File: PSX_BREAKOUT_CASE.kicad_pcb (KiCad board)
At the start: 2 copper layers, 100 x 71.1 mm, 11 parts

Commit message: Fixing Merging Error
Updated Case, moved connector, generated gerbers
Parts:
- removed the REF** at (118.4, 44.6)
- removed the REF** at (161.5, 44.8)
- removed the REF** at (178.0, 51.9)
- removed the REF** at (98.5, 62.7)
- added REF**: MountingHole_3.2mm_M3, MountingHole:MountingHole_3.2mm_M3, F.Cu at (162.2, 56.8)
- added REF**: MountingHole_3.2mm_M3, MountingHole:MountingHole_3.2mm_M3, F.Cu at (146.3, 45.6)
- added REF**: MountingHole_3.2mm_M3, MountingHole:MountingHole_3.2mm_M3, F.Cu at (109.7, 61.1)
- added REF**: MountingHole_3.2mm_M3, MountingHole:MountingHole_3.2mm_M3, F.Cu at (107.4, 45.8)
- moved REF** 16.6 mm to (162.2, 92.3)
- moved REF** 15.3 mm to (146.3, 81.2)
- moved REF** 11.4 mm to (109.7, 96.6)
- moved REF** 11.0 mm to (107.4, 81.4)
- moved G*** 10.7 mm to (129.3, 88.4)
- moved REF** 0.76 mm to (140.0, 59.4)
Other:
- outline, holes or cut-outs redrawn
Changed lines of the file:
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@@
-(kicad_pcb (version 20171130) (host pcbnew "(5.1.2)-1")
+(kicad_pcb (version 20171130) (host pcbnew "(5.1.0)-1")
   (general
     (thickness 1.6)
@@
       (drillshape 0)
       (scaleselection 1)
-      (outputdirectory "Gerbers/Case/"))
+      (outputdirectory "Gerbers/"))
   )
   (net 0 "")
@@
     (uvia_drill 0.1)
   )
+  (module MountingHole:MountingHole_3.2mm_M3 (layer F.Cu)
+    (at 162.179 56.769)
+    (descr "Mounting Hole 3.2mm, no annular, M3")
+    (tags "mounting hole 3.2mm no annular m3")
+    (attr virtual)
+    (fp_text reference REF** (at 0 -4.2) (layer F.SilkS) hide
+      (effects (font (size 1 1) (thickness 0.15)))
+    )
+    (fp_text value MountingHole_3.2mm_M3 (at 0 4.2) (layer F.Fab)
+      (effects (font (size 1 1) (thickness 0.15)))
+    )
+    (fp_text user %R (at 0.3 0) (layer F.Fab)
+      (effects (font (size 1 1) (thickness 0.15)))
+    )
+    (fp_circle (center 0 0) (end 3.2 0) (layer Cmts.User) (width 0.15))
+    (fp_circle (center 0 0) (end 3.45 0) (layer F.CrtYd) (width 0.05))
+    (pad 1 np_thru_hole circle (at 0 0) (size 3.2 3.2) (drill 3.2) (layers *.Cu *.Mask))
+  )
+  (module MountingHole:MountingHole_3.2mm_M3 (layer F.Cu)
+    (at 146.304 45.593)
+    (descr "Mounting Hole 3.2mm, no annular, M3")
+    (tags "mounting hole 3.2mm no annular m3")
+    (attr virtual)
+    (fp_text reference REF** (at 0 -4.2) (layer F.SilkS) hide
+      (effects (font (size 1 1) (thickness 0.15)))
+    )
+    (fp_text value MountingHole_3.2mm_M3 (at 0 4.2) (layer F.Fab)
+      (effects (font (size 1 1) (thickness 0.15)))
+    )
+    (fp_circle (center 0 0) (end 3.45 0) (layer F.CrtYd) (width 0.05))
+    (fp_circle (center 0 0) (end 3.2 0) (layer Cmts.User) (width 0.15))
+    (fp_text user %R (at 0.3 0) (layer F.Fab)
+      (effects (font (size 1 1) (thickness 0.15)))
+    )
+    (pad 1 np_thru_hole circle (at 0 0) (size 3.2 3.2) (drill 3.2) (layers *.Cu *.Mask))
+  )
+  (module MountingHole:MountingHole_3.2mm_M3 (layer F.Cu)
+    (at 109.728 61.087)
+    (descr "Mounting Hole 3.2mm, no annular, M3")
+    (tags "mounting hole 3.2mm no annular m3")
+    (attr virtual)
+    (fp_text reference REF** (at 0 -4.2) (layer F.SilkS) hide
+      (effects (font (size 1 1) (thickness 0.15)))
+    )
+    (fp_text value MountingHole_3.2mm_M3 (at 0 4.2) (layer F.Fab)
+      (effects (font (size 1 1) (thickness 0.15)))
+    )
+    (fp_circle (center 0 0) (end 3.45 0) (layer F.CrtYd) (width 0.05))
+    (fp_circle (center 0 0) (end 3.2 0) (layer Cmts.User) (width 0.15))
+    (fp_text user %R (at 0.3 0) (layer F.Fab)
+      (effects (font (size 1 1) (thickness 0.15)))
+    )
+    (pad 1 np_thru_hole circle (at 0 0) (size 3.2 3.2) (drill 3.2) (layers *.Cu *.Mask))
+  )
+  (module MountingHole:MountingHole_3.2mm_M3 (layer F.Cu)
+    (at 107.442 45.847)
+    (descr "Mounting Hole 3.2mm, no annular, M3")
+    (tags "mounting hole 3.2mm no annular m3")
+    (attr virtual)
+    (fp_text reference REF** (at 0 -4.2) (layer F.SilkS) hide
+      (effects (font (size 1 1) (thickness 0.15)))
+    )
+    (fp_text value MountingHole_3.2mm_M3 (at 0 4.2) (layer F.Fab)
+      (effects (font (size 1 1) (thickness 0.15)))
+    )
+    (fp_text user %R (at 0.3 0) (layer F.Fab)
+      (effects (font (size 1 1) (thickness 0.15)))
+    )
+    (fp_circle (center 0 0) (end 3.2 0) (layer Cmts.User) (width 0.15))
+    (fp_circle (center 0 0) (end 3.45 0) (layer F.CrtYd) (width 0.05))
+    (pad 1 np_thru_hole circle (at 0 0) (size 3.2 3.2) (drill 3.2) (layers *.Cu *.Mask))
+  )
   (module PSX_BREAKOUT:PSX_LOGO (layer F.Cu)
-    (at 139.954 88.44)
+    (at 129.286 88.44)
     (fp_text reference G*** (at 0 0) (layer F.SilkS) hide
       (effects (font (size 1.524 1.524) (thickness 0.3)))
@@
   )
   (module Symbol:OSHW-Symbol_33.5x30mm_Copper (layer B.Cu)
-    (at 139.954 58.674 180)
+    (at 139.954 59.436 180)
     (descr "Open Source Hardware Symbol")
     (tags "Logo Symbol OSHW")
@@
   )
   (module MountingHole:MountingHole_3.2mm_M3 (layer F.Cu)
-    (at 118.364 44.577)
+    (at 109.728 96.647)
     (descr "Mounting Hole 3.2mm, no annular, M3")
     (tags "mounting hole 3.2mm no annular m3")
@@
   )
   (module MountingHole:MountingHole_3.2mm_M3 (layer F.Cu)
-    (at 161.544 44.831)
+    (at 107.442 81.407)
     (descr "Mounting Hole 3.2mm, no annular, M3")
     (tags "mounting hole 3.2mm no annular m3")
@@
   )
   (module MountingHole:MountingHole_3.2mm_M3 (layer F.Cu)
-    (at 178.016 51.943)
+    (at 146.304 81.153)
     (descr "Mounting Hole 3.2mm, no annular, M3")
     (tags "mounting hole 3.2mm no annular m3")
@@
   )
   (module MountingHole:MountingHole_3.2mm_M3 (layer F.Cu)
-    (at 98.463 62.738)
+    (at 162.179 92.329)
     (descr "Mounting Hole 3.2mm, no annular, M3")
     (tags "mounting hole 3.2mm no annular m3")
@@
     (pad 1 np_thru_hole circle (at 0 0) (size 3.2 3.2) (drill 3.2) (layers *.Cu *.Mask))
   )
-  (module MountingHole:MountingHole_3.2mm_M3 (layer F.Cu)
-    (at 98.463 98.298)
-    (descr "Mounting Hole 3.2mm, no annular, M3")
-    (tags "mounting hole 3.2mm no annular m3")
-    (attr virtual)
-    (fp_text reference REF** (at 0 -4.2) (layer F.SilkS) hide
-      (effects (font (size 1 1) (thickness 0.15)))
-    )
-    (fp_text value MountingHole_3.2mm_M3 (at 0 4.2) (layer F.Fab)
-      (effects (font (size 1 1) (thickness 0.15)))
-    )
-    (fp_text user %R (at 0.3 0) (layer F.Fab)
-      (effects (font (size 1 1) (thickness 0.15)))
-    )
-    (fp_circle (center 0 0) (end 3.2 0) (layer Cmts.User) (width 0.15))
-    (fp_circle (center 0 0) (end 3.45 0) (layer F.CrtYd) (width 0.05))
-    (pad 1 np_thru_hole circle (at 0 0) (size 3.2 3.2) (drill 3.2) (layers *.Cu *.Mask))
-  )
-  (module MountingHole:MountingHole_3.2mm_M3 (layer F.Cu)
-    (at 118.364 80.137)
-    (descr "Mounting Hole 3.2mm, no annular, M3")
-    (tags "mounting hole 3.2mm no annular m3")
-    (attr virtual)
-    (fp_text reference REF** (at 0 -4.2) (layer F.SilkS) hide
-      (effects (font (size 1 1) (thickness 0.15)))
-    )
-    (fp_text value MountingHole_3.2mm_M3 (at 0 4.2) (layer F.Fab)
-      (effects (font (size 1 1) (thickness 0.15)))
-    )
-    (fp_circle (center 0 0) (end 3.45 0) (layer F.CrtYd) (width 0.05))
-    (fp_circle (center 0 0) (end 3.2 0) (layer Cmts.User) (width 0.15))
-    (fp_text user %R (at 0.3 0) (layer F.Fab)
-      (effects (font (size 1 1) (thickness 0.15)))
-    )
-    (pad 1 np_thru_hole circle (at 0 0) (size 3.2 3.2) (drill 3.2) (layers *.Cu *.Mask))
-  )
-  (module MountingHole:MountingHole_3.2mm_M3 (layer F.Cu)
-    (at 161.544 80.391)
-    (descr "Mounting Hole 3.2mm, no annular, M3")
-    (tags "mounting hole 3.2mm no annular m3")
-    (attr virtual)
-    (fp_text reference REF** (at 0 -4.2) (layer F.SilkS) hide
-      (effects (font (size 1 1) (thickness 0.15)))
-    )
-    (fp_text value MountingHole_3.2mm_M3 (at 0 4.2) (layer F.Fab)
-      (effects (font (size 1 1) (thickness 0.15)))
-    )
-    (fp_text user %R (at 0.3 0) (layer F.Fab)
-      (effects (font (size 1 1) (thickness 0.15)))
-    )
-    (fp_circle (center 0 0) (end 3.2 0) (layer Cmts.User) (width 0.15))
-    (fp_circle (center 0 0) (end 3.45 0) (layer F.CrtYd) (width 0.05))
-    (pad 1 np_thru_hole circle (at 0 0) (size 3.2 3.2) (drill 3.2) (layers *.Cu *.Mask))
-  )
-  (module MountingHole:MountingHole_3.2mm_M3 (layer F.Cu)
-    (at 178.016 87.503)
-    (descr "Mounting Hole 3.2mm, no annular, M3")
-    (tags "mounting hole 3.2mm no annular m3")
-    (attr virtual)
-    (fp_text reference REF** (at 0 -4.2) (layer F.SilkS) hide
-      (effects (font (size 1 1) (thickness 0.15)))
-    )
-    (fp_text value MountingHole_3.2mm_M3 (at 0 4.2) (layer F.Fab)
-      (effects (font (size 1 1) (thickness 0.15)))
-    )
-    (fp_circle (center 0 0) (end 3.45 0) (layer F.CrtYd) (width 0.05))
-    (fp_circle (center 0 0) (end 3.2 0) (layer Cmts.User) (width 0.15))
-    (fp_text user %R (at 0.3 0) (layer F.Fab)
-      (effects (font (size 1 1) (thickness 0.15)))
-    )
-    (pad 1 np_thru_hole circle (at 0 0) (size 3.2 3.2) (drill 3.2) (layers *.Cu *.Mask))
-  )
-  (gr_line (start 147.9735 97.26) (end 147.9735 111.76) (layer Edge.Cuts) (width 0.05))
-  (gr_line (start 189.954 97.26) (end 147.9735 97.26) (layer Edge.Cuts) (width 0.05))
+  (gr_line (start 147.9735 99.26) (end 147.9735 111.76) (layer Edge.Cuts) (width 0.05))
+  (gr_line (start 189.954 99.26) (end 147.9735 99.26) (layer Edge.Cuts) (width 0.05))
   (gr_line (start 132.461 40.64) (end 107.95 40.64) (layer Edge.Cuts) (width 0.05))
   (gr_line (start 132.461 40.64) (end 165.735 40.64) (layer Edge.Cuts) (width 0.05))
@@
     (effects (font (size 3 3) (thickness 0.15)))
   )
-  (gr_text 75Ω (at 110.236 77.724) (layer F.SilkS)
+  (gr_text 75Ω (at 125.476 77.724) (layer F.SilkS)
     (effects (font (size 1 1) (thickness 0.15)))
   )
-  (gr_text TTL (at 105.283 77.724) (layer F.SilkS)
+  (gr_text TTL (at 120.523 77.724) (layer F.SilkS)
     (effects (font (size 1 1) (thickness 0.15)))
   )
-  (gr_text "Sync Select\n↑CVBS\n●CSYNC\n↓LUMA" (at 156.591 90.17) (layer F.SilkS)
+  (gr_text "Sync Select\n↑CVBS\n●CSYNC\n↓LUMA" (at 166.878 87.122) (layer F.SilkS)
     (effects (font (size 2 2) (thickness 0.15)) (justify left))
   )
@@
   (gr_line (start 89.954 76.2) (end 89.954 111.76) (layer Edge.Cuts) (width 0.05))
   (gr_line (start 107.95 76.2) (end 89.954 76.2) (layer Edge.Cuts) (width 0.05))
-  (gr_line (start 189.954 76.2) (end 189.954 97.26) (layer Edge.Cuts) (width 0.05))
+  (gr_line (start 189.954 76.2) (end 189.954 99.26) (layer Edge.Cuts) (width 0.05))
   (gr_line (start 165.735 76.2) (end 189.954 76.2) (layer Edge.Cuts) (width 0.05))
   (gr_line (start 147.9735 111.76) (end 89.954 111.76) (layer Edge.Cuts) (width 0.05))

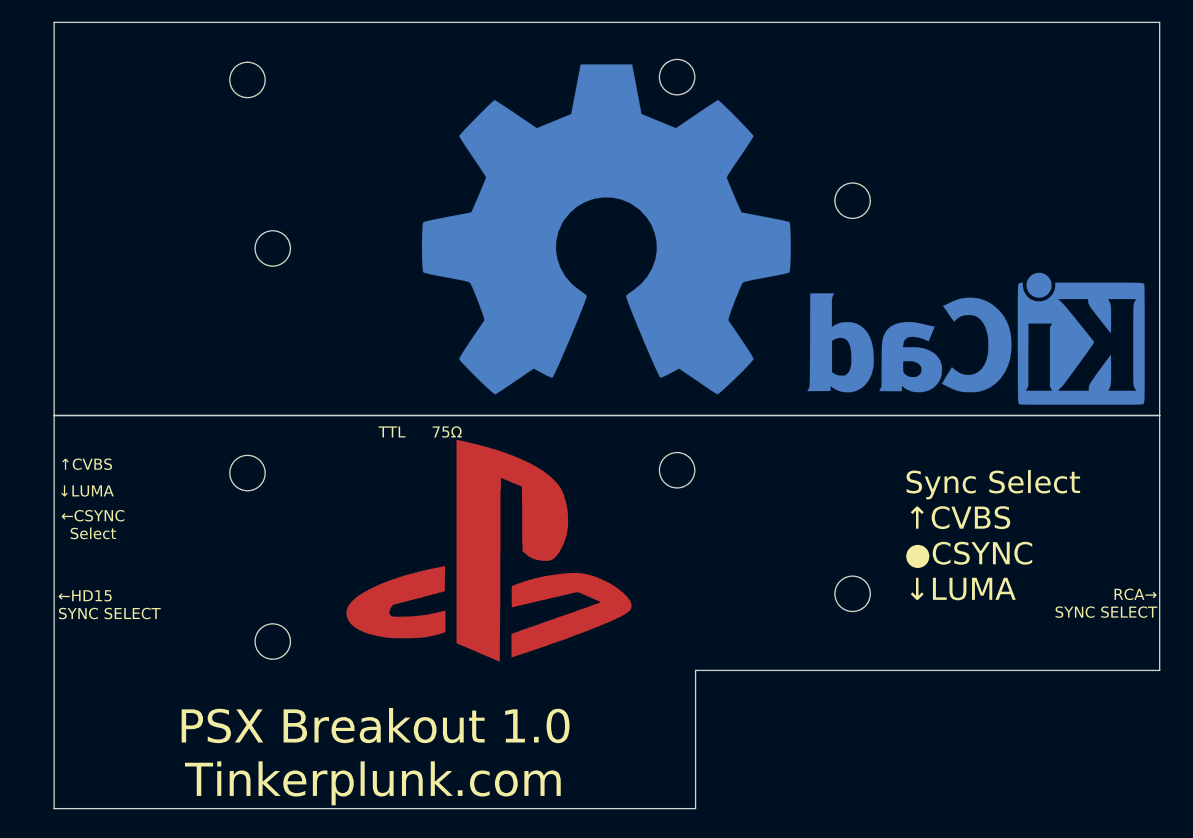
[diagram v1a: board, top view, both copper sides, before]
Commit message: Big Changes
Moved the csync selector switch to the right in order to move the hd15 connector back to the right position. Fixed hd15 footprint, moved screw holes and updated case with new screw holes and input labels. Updated 3d model for HD15 connector.
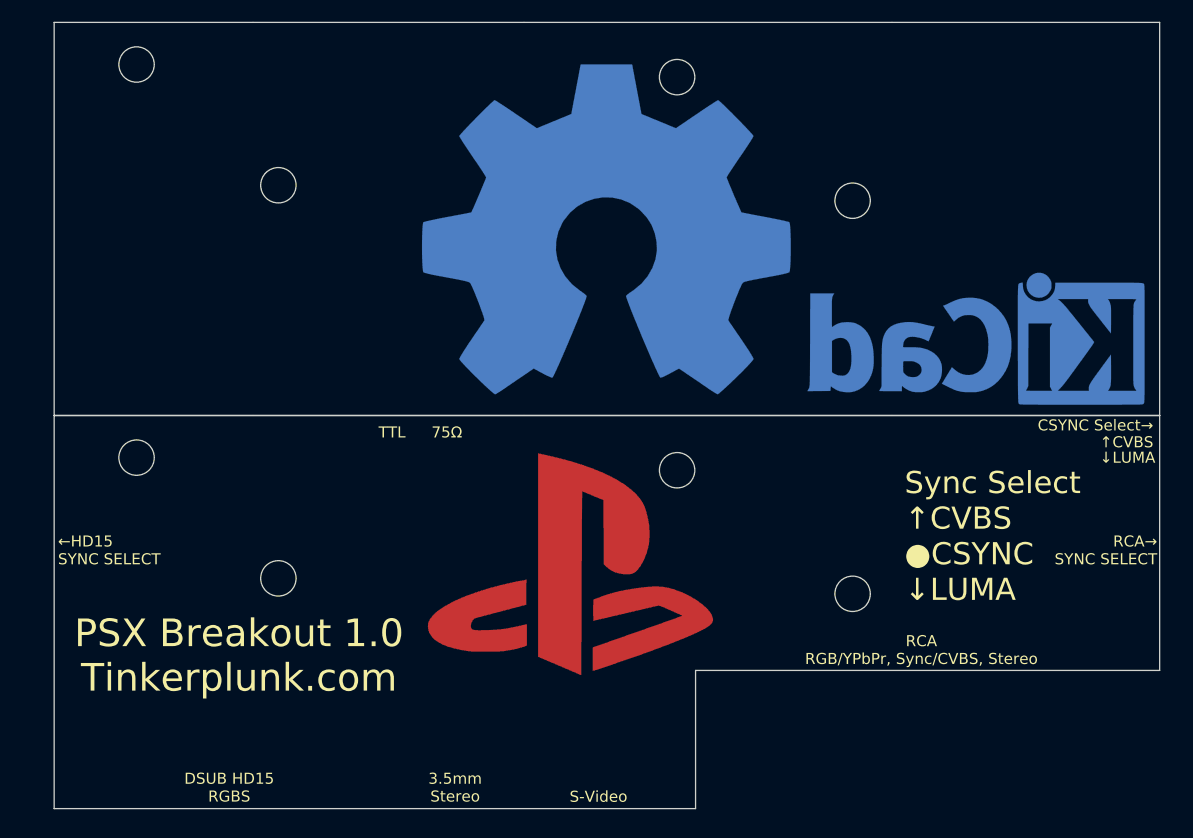
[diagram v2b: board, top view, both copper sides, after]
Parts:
- removed the REF** at (109.7, 61.1)
- removed the REF** at (107.4, 45.8)
- added REF**: MountingHole_3.2mm_M3, MountingHole:MountingHole_3.2mm_M3, F.Cu at (97.4, 44.5)
- added REF**: MountingHole_3.2mm_M3, MountingHole:MountingHole_3.2mm_M3, F.Cu at (110.2, 55.4)
- moved REF** 10.1 mm to (97.4, 80.0)
- moved G*** 7.47 mm to (136.7, 89.7)
- moved REF** 5.74 mm to (110.2, 90.9)
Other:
- board text added: "3.5mm Stereo"
- board text added: "CSYNC Select→"
- board text added: "DSUB HD15 RGBS"
- board text added: "RCA RGB/YPbPr, Sync/CVBS, Stereo"
- board text added: "S-Video"
- board text added: "←V-Score"
- board text removed: "←CSYNC Select"
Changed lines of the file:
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@@
   (general
     (thickness 1.6)
-    (drawings 26)
+    (drawings 31)
     (tracks 0)
     (zones 0)
@@
     (visible_elements 7FFFFFFF)
     (pcbplotparams
-      (layerselection 0x010f0_ffffffff)
+      (layerselection 0x012f0_ffffffff)
       (usegerberextensions true)
       (usegerberattributes false)
@@
   )
   (module MountingHole:MountingHole_3.2mm_M3 (layer F.Cu)
+    (at 97.409 44.45)
+    (descr "Mounting Hole 3.2mm, no annular, M3")
+    (tags "mounting hole 3.2mm no annular m3")
+    (attr virtual)
+    (fp_text reference REF** (at 0 -4.2) (layer F.SilkS) hide
+      (effects (font (size 1 1) (thickness 0.15)))
+    )
+    (fp_text value MountingHole_3.2mm_M3 (at 0 4.2) (layer F.Fab)
+      (effects (font (size 1 1) (thickness 0.15)))
+    )
+    (fp_text user %R (at 0.3 0) (layer F.Fab)
+      (effects (font (size 1 1) (thickness 0.15)))
+    )
+    (fp_circle (center 0 0) (end 3.2 0) (layer Cmts.User) (width 0.15))
+    (fp_circle (center 0 0) (end 3.45 0) (layer F.CrtYd) (width 0.05))
+    (pad 1 np_thru_hole circle (at 0 0) (size 3.2 3.2) (drill 3.2) (layers *.Cu *.Mask))
+  )
+  (module MountingHole:MountingHole_3.2mm_M3 (layer F.Cu)
+    (at 110.236 55.372)
+    (descr "Mounting Hole 3.2mm, no annular, M3")
+    (tags "mounting hole 3.2mm no annular m3")
+    (attr virtual)
+    (fp_text reference REF** (at 0 -4.2) (layer F.SilkS) hide
+      (effects (font (size 1 1) (thickness 0.15)))
+    )
+    (fp_text value MountingHole_3.2mm_M3 (at 0 4.2) (layer F.Fab)
+      (effects (font (size 1 1) (thickness 0.15)))
+    )
+    (fp_circle (center 0 0) (end 3.45 0) (layer F.CrtYd) (width 0.05))
+    (fp_circle (center 0 0) (end 3.2 0) (layer Cmts.User) (width 0.15))
+    (fp_text user %R (at 0.3 0) (layer F.Fab)
+      (effects (font (size 1 1) (thickness 0.15)))
+    )
+    (pad 1 np_thru_hole circle (at 0 0) (size 3.2 3.2) (drill 3.2) (layers *.Cu *.Mask))
+  )
+  (module MountingHole:MountingHole_3.2mm_M3 (layer F.Cu)
     (at 162.179 56.769)
     (descr "Mounting Hole 3.2mm, no annular, M3")
@@
     (pad 1 np_thru_hole circle (at 0 0) (size 3.2 3.2) (drill 3.2) (layers *.Cu *.Mask))
   )
-  (module MountingHole:MountingHole_3.2mm_M3 (layer F.Cu)
-    (at 109.728 61.087)
-    (descr "Mounting Hole 3.2mm, no annular, M3")
-    (tags "mounting hole 3.2mm no annular m3")
-    (attr virtual)
-    (fp_text reference REF** (at 0 -4.2) (layer F.SilkS) hide
-      (effects (font (size 1 1) (thickness 0.15)))
-    )
-    (fp_text value MountingHole_3.2mm_M3 (at 0 4.2) (layer F.Fab)
-      (effects (font (size 1 1) (thickness 0.15)))
-    )
-    (fp_circle (center 0 0) (end 3.45 0) (layer F.CrtYd) (width 0.05))
-    (fp_circle (center 0 0) (end 3.2 0) (layer Cmts.User) (width 0.15))
-    (fp_text user %R (at 0.3 0) (layer F.Fab)
-      (effects (font (size 1 1) (thickness 0.15)))
-    )
-    (pad 1 np_thru_hole circle (at 0 0) (size 3.2 3.2) (drill 3.2) (layers *.Cu *.Mask))
-  )
-  (module MountingHole:MountingHole_3.2mm_M3 (layer F.Cu)
-    (at 107.442 45.847)
-    (descr "Mounting Hole 3.2mm, no annular, M3")
-    (tags "mounting hole 3.2mm no annular m3")
-    (attr virtual)
-    (fp_text reference REF** (at 0 -4.2) (layer F.SilkS) hide
-      (effects (font (size 1 1) (thickness 0.15)))
-    )
-    (fp_text value MountingHole_3.2mm_M3 (at 0 4.2) (layer F.Fab)
-      (effects (font (size 1 1) (thickness 0.15)))
-    )
-    (fp_text user %R (at 0.3 0) (layer F.Fab)
-      (effects (font (size 1 1) (thickness 0.15)))
-    )
-    (fp_circle (center 0 0) (end 3.2 0) (layer Cmts.User) (width 0.15))
-    (fp_circle (center 0 0) (end 3.45 0) (layer F.CrtYd) (width 0.05))
-    (pad 1 np_thru_hole circle (at 0 0) (size 3.2 3.2) (drill 3.2) (layers *.Cu *.Mask))
-  )
   (module PSX_BREAKOUT:PSX_LOGO (layer F.Cu)
-    (at 129.286 88.44)
+    (at 136.652 89.662)
     (fp_text reference G*** (at 0 0) (layer F.SilkS) hide
       (effects (font (size 1.524 1.524) (thickness 0.3)))
@@
   )
   (module MountingHole:MountingHole_3.2mm_M3 (layer F.Cu)
-    (at 109.728 96.647)
+    (at 110.236 90.932)
     (descr "Mounting Hole 3.2mm, no annular, M3")
     (tags "mounting hole 3.2mm no annular m3")
@@
   )
   (module MountingHole:MountingHole_3.2mm_M3 (layer F.Cu)
-    (at 107.442 81.407)
+    (at 97.409 80.01)
     (descr "Mounting Hole 3.2mm, no annular, M3")
     (tags "mounting hole 3.2mm no annular m3")
@@
     )
     (pad 1 np_thru_hole circle (at 0 0) (size 3.2 3.2) (drill 3.2) (layers *.Cu *.Mask))
+  )
+  (gr_text ←V-Score (at 194.183 76.073) (layer Cmts.User)
+    (effects (font (size 1 1) (thickness 0.15)))
+  )
+  (gr_text "RCA\nRGB/YPbPr, Sync/CVBS, Stereo" (at 168.402 97.409) (layer F.SilkS)
+    (effects (font (size 1 1) (thickness 0.15)))
+  )
+  (gr_text S-Video (at 139.192 110.6805) (layer F.SilkS)
+    (effects (font (size 1 1) (thickness 0.15)))
+  )
+  (gr_text "3.5mm\nStereo" (at 126.227 109.855) (layer F.SilkS)
+    (effects (font (size 1 1) (thickness 0.15)))
+  )
+  (gr_text "DSUB HD15\nRGBS" (at 105.791 109.855) (layer F.SilkS)
+    (effects (font (size 1 1) (thickness 0.15)))
   )
   (gr_line (start 147.9735 99.26) (end 147.9735 111.76) (layer Edge.Cuts) (width 0.05))
@@
   (gr_line (start 189.954 76.2) (end 89.954 76.2) (layer Edge.Cuts) (width 0.05))
   (gr_line (start 107.95 40.64) (end 89.954 40.64) (layer Edge.Cuts) (width 0.05))
-  (gr_text "Licensed under CERN OHL 1.2\nhttps://github.com/arithmaldor" (at 138.684 53.213) (layer B.SilkS)
+  (gr_text "Licensed under CERN OHL 1.2\nhttps://github.com/arithmaldor" (at 116.078 70.358) (layer B.SilkS)
     (effects (font (size 2 2) (thickness 0.15)) (justify mirror))
   )
-  (gr_text "PSX Breakout 1.0\nTinkerplunk.com" (at 118.96375 106.807) (layer F.SilkS)
-    (effects (font (size 3 3) (thickness 0.15)))
+  (gr_text "PSX Breakout 1.0\nTinkerplunk.com" (at 106.68 97.917) (layer F.SilkS)
+    (effects (font (size 2.5 2.5) (thickness 0.15)))
   )
   (gr_text 75Ω (at 125.476 77.724) (layer F.SilkS)
@@
     (effects (font (size 2 2) (thickness 0.15)) (justify left))
   )
-  (gr_text "RCA→\nSYNC SELECT" (at 189.738 93.218) (layer F.SilkS)
+  (gr_text "RCA→\nSYNC SELECT" (at 189.738 88.392) (layer F.SilkS)
     (effects (font (size 1 1) (thickness 0.15)) (justify right))
   )
-  (gr_text "←HD15\nSYNC SELECT" (at 90.297 93.345) (layer F.SilkS)
+  (gr_text "←HD15\nSYNC SELECT" (at 90.297 88.392) (layer F.SilkS)
     (effects (font (size 1 1) (thickness 0.15)) (justify left))
   )
-  (gr_text ↓LUMA (at 92.837 83.058) (layer F.SilkS)
+  (gr_text ↓LUMA (at 184.531 80.01) (layer F.SilkS)
+    (effects (font (size 1 1) (thickness 0.15)) (justify left))
+  )
+  (gr_text "CSYNC Select→" (at 184.15 77.089) (layer F.SilkS)
     (effects (font (size 1 1) (thickness 0.15)))
   )
-  (gr_text "←CSYNC\nSelect" (at 93.472 86.106) (layer F.SilkS)
-    (effects (font (size 1 1) (thickness 0.15)))
-  )
-  (gr_text ↑CVBS (at 92.837 80.645) (layer F.SilkS)
-    (effects (font (size 1 1) (thickness 0.15)))
+  (gr_text ↑CVBS (at 184.531 78.613) (layer F.SilkS)
+    (effects (font (size 1 1) (thickness 0.15)) (justify left))
   )
   (gr_line (start 89.954 76.2) (end 89.954 111.76) (layer Edge.Cuts) (width 0.05))
